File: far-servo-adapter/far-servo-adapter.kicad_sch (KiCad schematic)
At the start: 24 parts, among them J1 Screw_Terminal_01x02, J2 Screw_Terminal_01x02, J3 Screw_Terminal_01x02, J4 Screw_Terminal_01x02, Q1 BTA16-600BW, Q2 BTA16-600BW, Q3 BTA16-600BW, Q4 BTA16-600BW, U1 MOC3063M, U2 MOC3063M, U3 MOC3063M, U4 MOC3063M

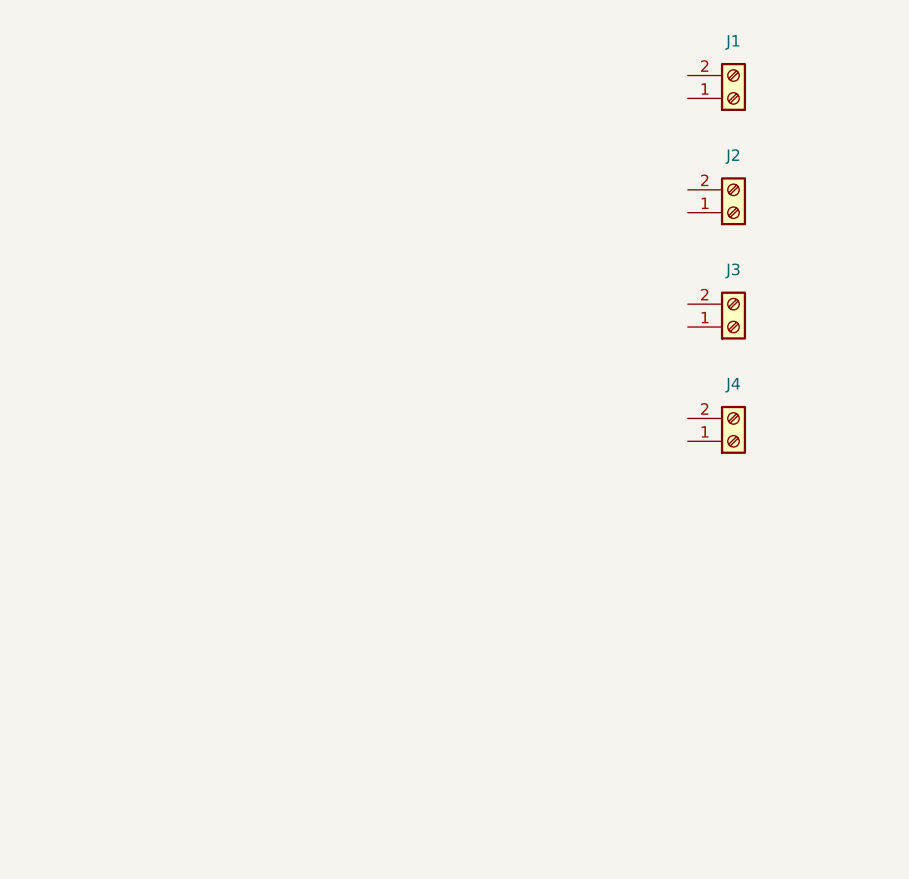
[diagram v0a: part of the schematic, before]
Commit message: far-servo-adapter += terminals
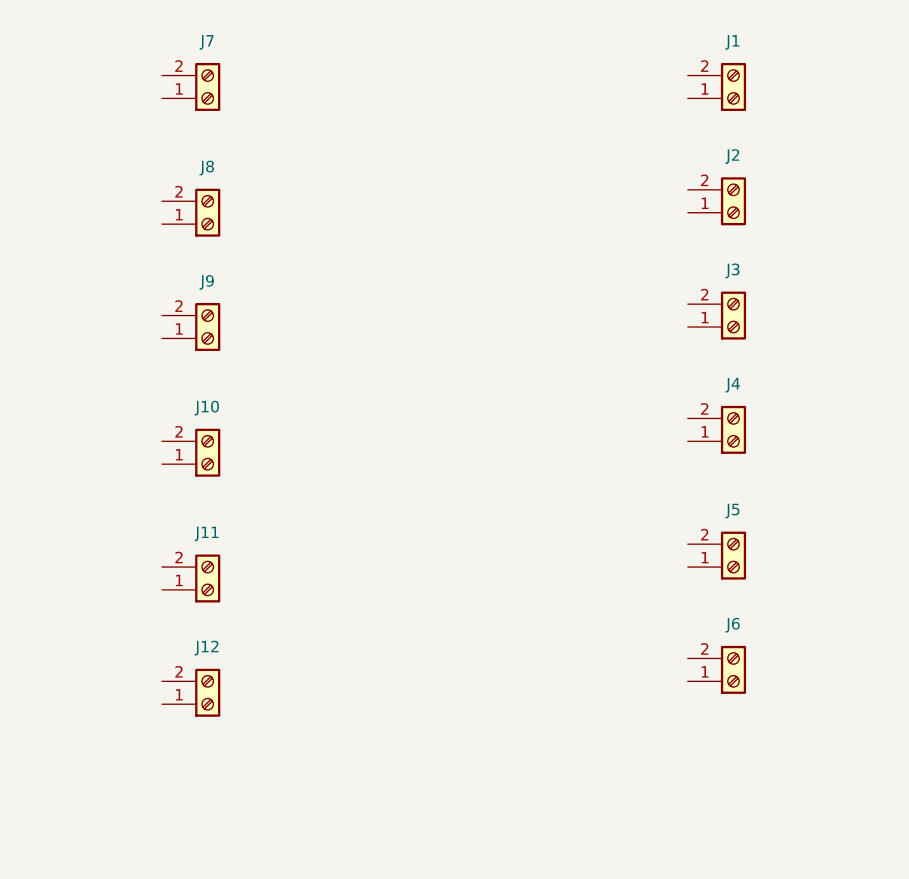
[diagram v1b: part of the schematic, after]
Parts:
- added J10, J11, J12, J5, J6, J7, J8, J9: Screw_Terminal_01x02, TerminalBlock_Phoenix:TerminalBlock_Phoenix_MKDS-1,5-2_1x02_P5.00mm_Horizontal, symbol Connector:Screw_Terminal_01x02
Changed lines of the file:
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@@
     (effects (font (size 1.27 1.27)) (justify left bottom))
+  )
+  (symbol (lib_id "Connector:Screw_Terminal_01x02") (at 265.43 81.28 0) (mirror x) (unit 1)
+    (in_bom yes) (on_board yes) (dnp no) (fields_autoplaced)
+    (property "Reference" "J5" (at 265.43 74.93 0)
+      (effects (font (size 1.27 1.27)))
+    )
+    (property "Value" "Screw_Terminal_01x02" (at 267.97 78.7401 0)
+      (effects (font (size 1.27 1.27)) (justify left) hide)
+    )
+    (property "Footprint" "TerminalBlock_Phoenix:TerminalBlock_Phoenix_MKDS-1,5-2_1x02_P5.00mm_Horizontal" (at 265.43 81.28 0)
+      (effects (font (size 1.27 1.27)) hide)
+    )
+    (property "Datasheet" "~" (at 265.43 81.28 0)
+      (effects (font (size 1.27 1.27)) hide)
+    )
+    (pin "1")
+    (pin "2")
+    (instances
+      (project "far-servo-adapter"
+        (path "/a4be5700-2f7f-47cf-a182-7dd562a5cec8"
+          (reference "J5") (unit 1)
+        )
+      )
+    )
   )
   (symbol (lib_id "Relay_SolidState:MOC3063M") (at 106.68 27.94 0) (unit 1)
@@
     )
   )
+  (symbol (lib_id "Connector:Screw_Terminal_01x02") (at 207.01 55.88 0) (mirror x) (unit 1)
+    (in_bom yes) (on_board yes) (dnp no) (fields_autoplaced)
+    (property "Reference" "J9" (at 207.01 49.53 0)
+      (effects (font (size 1.27 1.27)))
+    )
+    (property "Value" "Screw_Terminal_01x02" (at 209.55 53.3401 0)
+      (effects (font (size 1.27 1.27)) (justify left) hide)
+    )
+    (property "Footprint" "TerminalBlock_Phoenix:TerminalBlock_Phoenix_MKDS-1,5-2_1x02_P5.00mm_Horizontal" (at 207.01 55.88 0)
+      (effects (font (size 1.27 1.27)) hide)
+    )
+    (property "Datasheet" "~" (at 207.01 55.88 0)
+      (effects (font (size 1.27 1.27)) hide)
+    )
+    (pin "1")
+    (pin "2")
+    (instances
+      (project "far-servo-adapter"
+        (path "/a4be5700-2f7f-47cf-a182-7dd562a5cec8"
+          (reference "J9") (unit 1)
+        )
+      )
+    )
+  )
   (symbol (lib_id "Device:R") (at 120.65 50.8 90) (unit 1)
     (in_bom yes) (on_board yes) (dnp no)
@@
         (path "/a4be5700-2f7f-47cf-a182-7dd562a5cec8"
           (reference "R3") (unit 1)
+        )
+      )
+    )
+  )
+  (symbol (lib_id "Connector:Screw_Terminal_01x02") (at 207.01 69.85 0) (mirror x) (unit 1)
+    (in_bom yes) (on_board yes) (dnp no) (fields_autoplaced)
+    (property "Reference" "J10" (at 207.01 63.5 0)
+      (effects (font (size 1.27 1.27)))
+    )
+    (property "Value" "Screw_Terminal_01x02" (at 209.55 67.3101 0)
+      (effects (font (size 1.27 1.27)) (justify left) hide)
+    )
+    (property "Footprint" "TerminalBlock_Phoenix:TerminalBlock_Phoenix_MKDS-1,5-2_1x02_P5.00mm_Horizontal" (at 207.01 69.85 0)
+      (effects (font (size 1.27 1.27)) hide)
+    )
+    (property "Datasheet" "~" (at 207.01 69.85 0)
+      (effects (font (size 1.27 1.27)) hide)
+    )
+    (pin "1")
+    (pin "2")
+    (instances
+      (project "far-servo-adapter"
+        (path "/a4be5700-2f7f-47cf-a182-7dd562a5cec8"
+          (reference "J10") (unit 1)
         )
       )
@@
     )
   )
+  (symbol (lib_id "Connector:Screw_Terminal_01x02") (at 207.01 83.82 0) (mirror x) (unit 1)
+    (in_bom yes) (on_board yes) (dnp no) (fields_autoplaced)
+    (property "Reference" "J11" (at 207.01 77.47 0)
+      (effects (font (size 1.27 1.27)))
+    )
+    (property "Value" "Screw_Terminal_01x02" (at 209.55 81.2801 0)
+      (effects (font (size 1.27 1.27)) (justify left) hide)
+    )
+    (property "Footprint" "TerminalBlock_Phoenix:TerminalBlock_Phoenix_MKDS-1,5-2_1x02_P5.00mm_Horizontal" (at 207.01 83.82 0)
+      (effects (font (size 1.27 1.27)) hide)
+    )
+    (property "Datasheet" "~" (at 207.01 83.82 0)
+      (effects (font (size 1.27 1.27)) hide)
+    )
+    (pin "1")
+    (pin "2")
+    (instances
+      (project "far-servo-adapter"
+        (path "/a4be5700-2f7f-47cf-a182-7dd562a5cec8"
+          (reference "J11") (unit 1)
+        )
+      )
+    )
+  )
   (symbol (lib_id "Device:Varistor") (at 143.51 27.94 0) (unit 1)
     (in_bom yes) (on_board yes) (dnp no)
@@
         (path "/a4be5700-2f7f-47cf-a182-7dd562a5cec8"
           (reference "RV3") (unit 1)
+        )
+      )
+    )
+  )
+  (symbol (lib_id "Connector:Screw_Terminal_01x02") (at 207.01 29.21 0) (mirror x) (unit 1)
+    (in_bom yes) (on_board yes) (dnp no) (fields_autoplaced)
+    (property "Reference" "J7" (at 207.01 22.86 0)
+      (effects (font (size 1.27 1.27)))
+    )
+    (property "Value" "Screw_Terminal_01x02" (at 209.55 26.6701 0)
+      (effects (font (size 1.27 1.27)) (justify left) hide)
+    )
+    (property "Footprint" "TerminalBlock_Phoenix:TerminalBlock_Phoenix_MKDS-1,5-2_1x02_P5.00mm_Horizontal" (at 207.01 29.21 0)
+      (effects (font (size 1.27 1.27)) hide)
+    )
+    (property "Datasheet" "~" (at 207.01 29.21 0)
+      (effects (font (size 1.27 1.27)) hide)
+    )
+    (pin "1")
+    (pin "2")
+    (instances
+      (project "far-servo-adapter"
+        (path "/a4be5700-2f7f-47cf-a182-7dd562a5cec8"
+          (reference "J7") (unit 1)
         )
       )
@@
     )
   )
+  (symbol (lib_id "Connector:Screw_Terminal_01x02") (at 207.01 43.18 0) (mirror x) (unit 1)
+    (in_bom yes) (on_board yes) (dnp no) (fields_autoplaced)
+    (property "Reference" "J8" (at 207.01 36.83 0)
+      (effects (font (size 1.27 1.27)))
+    )
+    (property "Value" "Screw_Terminal_01x02" (at 209.55 40.6401 0)
+      (effects (font (size 1.27 1.27)) (justify left) hide)
+    )
+    (property "Footprint" "TerminalBlock_Phoenix:TerminalBlock_Phoenix_MKDS-1,5-2_1x02_P5.00mm_Horizontal" (at 207.01 43.18 0)
+      (effects (font (size 1.27 1.27)) hide)
+    )
+    (property "Datasheet" "~" (at 207.01 43.18 0)
+      (effects (font (size 1.27 1.27)) hide)
+    )
+    (pin "1")
+    (pin "2")
+    (instances
+      (project "far-servo-adapter"
+        (path "/a4be5700-2f7f-47cf-a182-7dd562a5cec8"
+          (reference "J8") (unit 1)
+        )
+      )
+    )
+  )
   (symbol (lib_id "Device:R") (at 120.65 25.4 90) (unit 1)
     (in_bom yes) (on_board yes) (dnp no)
@@
         (path "/a4be5700-2f7f-47cf-a182-7dd562a5cec8"
           (reference "Q1") (unit 1)
+        )
+      )
+    )
+  )
+  (symbol (lib_id "Connector:Screw_Terminal_01x02") (at 265.43 93.98 0) (mirror x) (unit 1)
+    (in_bom yes) (on_board yes) (dnp no) (fields_autoplaced)
+    (property "Reference" "J6" (at 265.43 87.63 0)
+      (effects (font (size 1.27 1.27)))
+    )
+    (property "Value" "Screw_Terminal_01x02" (at 267.97 91.4401 0)
+      (effects (font (size 1.27 1.27)) (justify left) hide)
+    )
+    (property "Footprint" "TerminalBlock_Phoenix:TerminalBlock_Phoenix_MKDS-1,5-2_1x02_P5.00mm_Horizontal" (at 265.43 93.98 0)
+      (effects (font (size 1.27 1.27)) hide)
+    )
+    (property "Datasheet" "~" (at 265.43 93.98 0)
+      (effects (font (size 1.27 1.27)) hide)
+    )
+    (pin "1")
+    (pin "2")
+    (instances
+      (project "far-servo-adapter"
+        (path "/a4be5700-2f7f-47cf-a182-7dd562a5cec8"
+          (reference "J6") (unit 1)
         )
       )
@@
         )
       )
+    )
+  )
+  (symbol (lib_id "Connector:Screw_Terminal_01x02") (at 207.01 96.52 0) (mirror x) (unit 1)
+    (in_bom yes) (on_board yes) (dnp no) (fields_autoplaced)
+    (property "Reference" "J12" (at 207.01 90.17 0)
+      (effects (font (size 1.27 1.27)))
+    )
+    (property "Value" "Screw_Terminal_01x02" (at 209.55 93.9801 0)
+      (effects (font (size 1.27 1.27)) (justify left) hide)
+    )
+    (property "Footprint" "TerminalBlock_Phoenix:TerminalBlock_Phoenix_MKDS-1,5-2_1x02_P5.00mm_Horizontal" (at 207.01 96.52 0)
+      (effects (font (size 1.27 1.27)) hide)
+    )
+    (property "Datasheet" "~" (at 207.01 96.52 0)
+      (effects (font (size 1.27 1.27)) hide)
+    )
+    (pin "1")
+    (pin "2")
+    (instances
+      (project "far-servo-adapter"
+        (path "/a4be5700-2f7f-47cf-a182-7dd562a5cec8"
+          (reference "J12") (unit 1)
+        )
+      )

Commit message: update
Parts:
- added C1, C2, C3, C4: C_Polarized, Capacitor_THT:CP_Radial_D5.0mm_P2.50mm, symbol Device:C_Polarized
- added R10, R15, R16, R5, R6, R7, R8, R9: 100k, Resistor_THT:R_Axial_DIN0516_L15.5mm_D5.0mm_P20.32mm_Horizontal, symbol Device:R
- added TP1, TP2, TP4, TP5, TP6, TP7, TP8, TP9: TestPoint, Connector_Pin:Pin_D1.0mm_L10.0mm, symbol Connector:TestPoint
- added U5, U6, U7, U8: PC814, Package_DIP:DIP-4_W7.62mm, symbol Isolator:SFH620A-1
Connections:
- net IN1: now also J7.2 (Pin_2)
- net IN2: now also J7.1 (Pin_1)
- net IN3: now also J8.1 (Pin_1)
- net IN4: now also J9.2 (Pin_2)
- net LSENS1: now reaches J5.1 (Pin_1)
- net LSENS1: now also R5.1
- net LSENS2: now reaches J5.2 (Pin_2)
- net LSENS2: now also R7.1
- net L1: now reaches J1.1 (Pin_1)
- net L1: now also Q1.1 (A1), RV1.2
- net L2: now reaches J1.2 (Pin_2)
- net L2: now also Q2.1 (A1), RV2.2
- net IPOS2: now reaches J9.1 (Pin_1)
- net IPOS2: now also U3.1, U4.1, TP2.1
- net L: now reaches Q3.2 (A2), R3.2, RV3.1
- net L: now also J3.1 (Pin_1), Q1.2 (A2), Q2.2 (A2), Q4.2 (A2), R1.2, R2.2, R4.2, RV1.1, RV2.1, RV4.1, TP4.1, TP5.1, TP6.1, TP7.1, TP8.1, TP9.1
- net SENS2: now reaches J10.1 (Pin_1)
- net SENS2: now also C2.1, U6.4
- net SENS1: now reaches J10.2 (Pin_2)
- net SENS1: now also C1.1, U5.4
- net L3: now reaches J2.1 (Pin_1)
- net L3: now also Q3.1 (A1), RV3.2
- net L4: now reaches J2.2 (Pin_2)
- net L4: now also Q4.1 (A1), RV4.2
- net N: now reaches J3.2 (Pin_2)
- net N: now also J4.1 (Pin_1), J4.2 (Pin_2), R10.1, R16.1, R6.1, R8.1
- net SENS3: now reaches J11.1 (Pin_1)
- net SENS3: now also C3.1, U7.4
- net NEG: now reaches J11.2 (Pin_2)
- net NEG: now also J12.1 (Pin_1), C1.2, C2.2, C3.2, C4.2, U5.3, U6.3, U7.3, U8.3
- net IPOS1: now reaches J8.2 (Pin_2)
- net IPOS1: now also U1.1, U2.1, TP1.1
- net LSENS3: now reaches J6.1 (Pin_1)
- net LSENS3: now also R9.1
- net LSENS4: now reaches J6.2 (Pin_2)
- net LSENS4: now also R15.1
- net SENS4: now reaches J12.2 (Pin_2)
- net SENS4: now also C4.1, U8.4
- removed net VHL: U1.1, U2.1, U3.1, U4.1
- new net: R7.2, U6.1
- new net: R8.2, U6.2
- new net: R5.2, U5.1
- new net: R9.2, U7.1
- new net: R10.2, U7.2
- new net: R6.2, U5.2
- new net: R16.2, U8.2
- new net: R15.2, U8.1
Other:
- moved on the sheet: Q3, Q4, R13, R14, R3, R4, U3, U4
